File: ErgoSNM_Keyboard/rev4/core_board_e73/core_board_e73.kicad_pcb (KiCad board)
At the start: 2 copper layers, 68.5 x 53 mm, 60 parts, among them J1 USB_C_Receptacle_USB2.0, J2 Conn_02x10_Odd_Even, J3 Conn_02x10_Odd_Even, J4 PJ-393_TRRS_8P, J5 PJ-393_TRRS_8P, J6 Conn_Batt, J7 Debug, J8 Conn_02x05_Odd_Even, J9 Conn_02x05_Odd_Even, SW1 SW_SPDT, SW2 SW_SPDT, U1 E73-2G4M08S1C, U2 USBLC6-2SC6, U3 BQ24075RGT, U4 TPS63900, Y1 32.768kHz

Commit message: feat: update the connectors of the main board and core board
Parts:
- removed LD1: BLUE, LED_SMD:LED_0603_1608Metric
- removed LD2: RED, LED_SMD:LED_0603_1608Metric
- moved R11 24.9 mm to (133.5, 94.6), turned to 180 degrees
- moved R6 21.5 mm to (133.5, 95.8), turned to 180 degrees
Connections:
- J2 pad 18: unconnected-(J2-Pin_18-Pad18) -> CHG_LED
- J2 pad 2: unconnected-(J2-Pin_2-Pad2) -> STATUS_LED
- J2 pad 20: unconnected-(J2-Pin_20-Pad20) -> STATUS_LED
- J2 pad 4: unconnected-(J2-Pin_4-Pad4) -> CHG_LED
- R11 pad 1: VDDH -> CHG_LED
- R11 pad 2: Net-(LD2-A) -> Net-(U3-~{CHG})
- R6 pad 2: Net-(LD1-A) -> Net-(U1-P0.15)
- U1 pad 28: STATUS_LED -> Net-(U1-P0.15)
- U3 pad 9: Net-(LD2-K) -> Net-(U3-~{CHG})
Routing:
- net STATUS_LED: track 78.8 -> 16.6 mm, vias 2 -> 1
- net Net-(U3-~{CHG}): track 0.00 -> 27.4 mm, vias 0 -> 2
- net Net-(LD2-K): track 21.3 -> 0.00 mm, vias 2 -> 0
- net VDDH: track 25.8 -> 9.07 mm, vias 3 -> 2
- net Net-(U1-P0.15): track 0.00 -> 15.5 mm, vias 0 -> 2
- net CHG_LED: track 0.00 -> 15.3 mm, vias 0 -> 1
- net GND: track 42.0 -> 46.9 mm
- net Net-(LD2-A): track 1.40 -> 0.00 mm
- net Net-(LD1-A): track 1.36 -> 0.00 mm
- net COL_IO_5: track 20.0 -> 20.9 mm
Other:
- outline, holes or cut-outs redrawn

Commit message: feat: update E73 core board
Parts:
- removed H23, H5, H6, H7: MountingHole, ErgoSNM_Keyboard:mouse_bit
- removed H3, H4: MountingHole, MountingHole:MountingHole_2.7mm_M2.5_ISO7380
- removed J8, J9: Conn_02x05_Odd_Even, Connector_PinHeader_1.27mm:PinHeader_2x04_P1.27mm_Vertical
- removed the SB3 at (154.1, 92.6)
- removed the TP1 at (155.2, 117.8)
- added R14: 0R, Resistor_SMD:R_0603_1608Metric, F.Cu at (170.1, 103.3)
- added R15: 0R, Resistor_SMD:R_0603_1608Metric, F.Cu at (170.1, 101.8)
- added R18: 0R, Resistor_SMD:R_0603_1608Metric, F.Cu at (163.5, 119.1)
- added R8: 0R, Resistor_SMD:R_0603_1608Metric, F.Cu at (161.2, 104.1)
- added R9: 0R, Resistor_SMD:R_0603_1608Metric, F.Cu at (166.3, 108.2)
- added SB2: LiPo_CHG, Jumper:SolderJumper-2_P1.3mm_Open_TrianglePad1.0x1.5mm, B.Cu at (160.2, 102.6)
- J2, J3: footprint Connector_PinHeader_1.27mm:PinHeader_2x10_P1.27mm_Vertical_SMD -> Connector_PinHeader_1.27mm:PinHeader_2x10_P1.27mm_Vertical
- J7: footprint ErgoSNM_Keyboard:SWD 10pin -> Connector_PinHeader_1.27mm:PinHeader_2x05_P1.27mm_Vertical; moved to F.Cu
- R16: renamed from R12; value 1.2k 1% -> 15k 1%
- R19: renamed from R14; value 30k 1% -> 20k 1%
- SB3: renamed from SB2; value LiPo_CHG -> LiPo_BATT
- TP1: renamed from TP2; moved to F.Cu
- U1: footprint ErgoSNM_Keyboard:E73-2G4M08S1C-52840_PCBA -> ErgoSNM_Keyboard:E73-2G4M08S1C-52840_Hand
- moved R13 33.7 mm to (166.5, 101.1)
- moved C5 22.2 mm to (146.7, 123.7), turned to -90 degrees
- moved R19 22.0 mm to (159.4, 113.5)
- moved C11 21.8 mm to (163.5, 111.5)
- moved C12 21.8 mm to (163.5, 117.0)
- moved L1 21.8 mm to (167.1, 114.3)
- moved U4 21.8 mm to (163.5, 114.3)
- moved R17 21.8 mm to (159.4, 115.0)
- moved SB4 21.7 mm to (159.1, 114.2)
- moved R16 21.6 mm to (159.4, 116.5)
- moved C6 20.6 mm to (146.7, 121.6), turned to 90 degrees
- moved SB1 20.1 mm to (160.2, 105.4), turned to 180 degrees
- moved Y1 19.3 mm to (145.0, 122.7), turned to 90 degrees
- moved R10 18.8 mm to (146.2, 119.3), turned to -90 degrees
- moved R12 18.3 mm to (161.7, 106.4)
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- renumbered R8 to R10, R9 to R11, R10 to R12, R11 to R13, R13 to R17, R6 to R5, R5 to R6
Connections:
- net /CONN_D+ renamed /power/CONN_D+
- net /CONN_D- renamed /power/CONN_D-
- net /OUT_SEL renamed /power/OUT_SEL
- net /USB_SH renamed /power/USB_SH
- net /VBATT_SRC renamed /power/VBATT_SRC
- net /VIN_DCDC renamed /power/VIN_DCDC
- C12 pad 1: VDD -> /power/VOUT_DCDC
- C7 pad 1: VBUS -> Net-(SB2-A)
- U1 pad 10: COL_IO_2 -> COL_IO_0
- U1 pad 15: COL_IO_3 -> unconnected-(U1-P0.05-Pad15)
- U1 pad 17: COL_IO_4 -> unconnected-(U1-P1.09-Pad17)
- U1 pad 22: COL_IO_5 -> unconnected-(U1-P0.07-Pad22)
- U1 pad 30: HS_IO_4 -> HS_IO_1
- U1 pad 32: HS_IO_3 -> HS_IO_2
- U1 pad 34: HS_IO_2 -> HS_IO_3
- U1 pad 35: HS_IO_1 -> HS_IO_5
- U1 pad 36: HS_IO_5 -> HS_IO_4
- U1 pad 38: unconnected-(U1-P1.02-Pad38) -> COL_IO_3
- U1 pad 40: unconnected-(U1-P1.04-Pad40) -> COL_IO_4
- U1 pad 42: unconnected-(U1-P1.06-Pad42) -> COL_IO_5
- U1 pad 8: COL_IO_0 -> COL_IO_2
- U3 pad 13: VBUS -> Net-(SB2-A)
- U3 pad 15: GND -> Net-(U3-SYSOFF)
- U3 pad 4: GND -> Net-(U3-~{CE})
- U4 pad 6: VDD -> /power/VOUT_DCDC
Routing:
- net CHG_LED: track 15.3 -> 59.7 mm
- net ROW_IO_0: track 26.5 -> 58.8 mm
- net ROW_IO_1: track 25.6 -> 56.9 mm
- net ROW_IO_4: track 19.2 -> 50.0 mm
- net ROW_IO_5: track 17.8 -> 48.1 mm
- net ROW_IO_2: track 24.8 -> 55.0 mm
- net ROW_IO_3: track 23.9 -> 53.1 mm
- net RX: track 115.8 -> 86.7 mm, vias 4 -> 2
- net Net-(U3-~{CHG}): track 27.4 -> 1.62 mm, vias 2 -> 0
- net VDD: track 103.9 -> 129.5 mm, vias 3 -> 1
- net HS_IO_5: track 5.64 -> 30.1 mm
- net COL_IO_2: track 20.2 -> 43.1 mm
- net TX: track 117.6 -> 96.0 mm, vias 4 -> 2
- net RESET: track 57.0 -> 76.3 mm, vias 1 -> 4
- net COL_IO_1: track 20.8 -> 38.5 mm
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- added copper zone on F.Cu, net /power/VOUT_DCDC
- removed copper zone on F.Cu, net VDD
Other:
- board size 68.5 x 53 mm -> 48.3 x 49.5 mm
- board text added: "BAT"
- board text added: "ErgoSNM Rev4.0 Core Board (E73)"
- board text added: "USB"
- board text removed: "CHG"
- board text removed: "Core Board"
- board text removed: "ErgoSNM"
- board text removed: "L"
- board text removed: "OFF"
- board text removed: "ON"
- board text removed: "R"
- board text removed: "Rev${REVISION}"
- board text removed: "STA"
- board text removed: "Unit: mm"

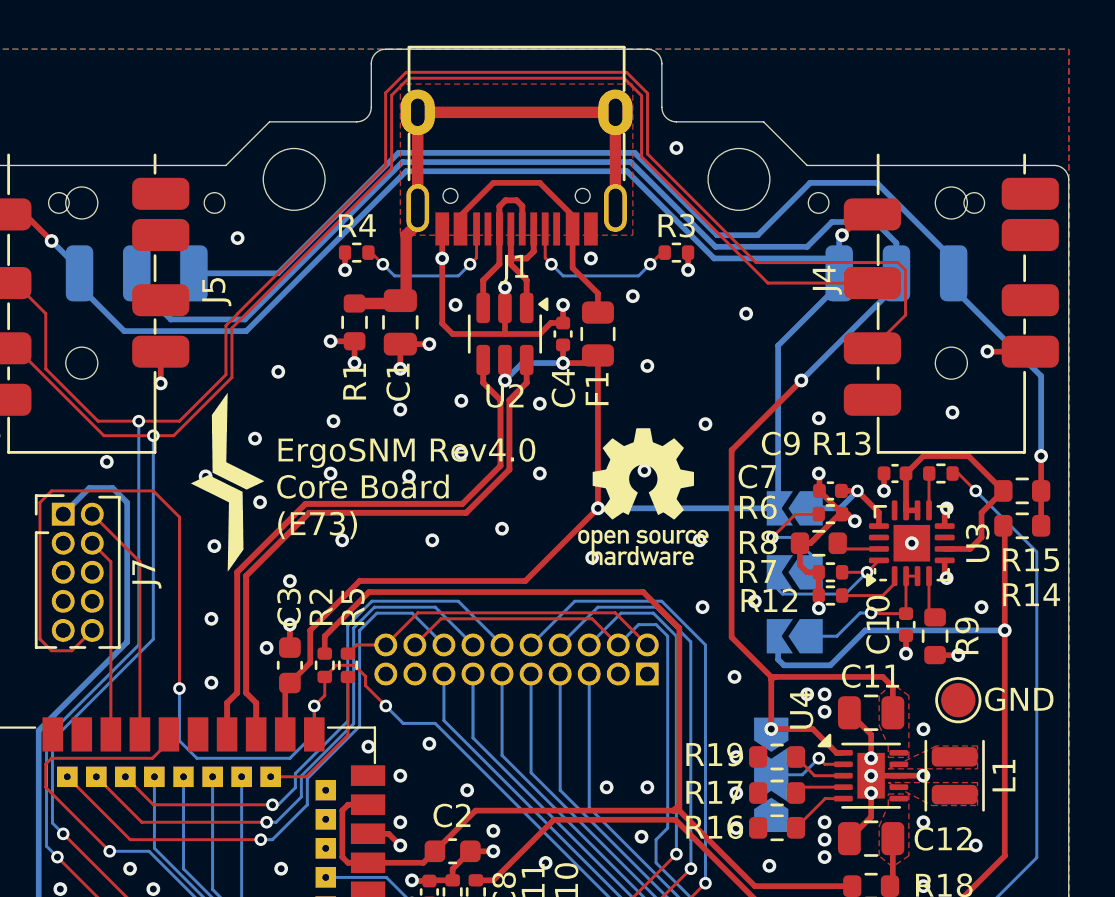
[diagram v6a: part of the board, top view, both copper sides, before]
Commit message: feat: add stats and change LED
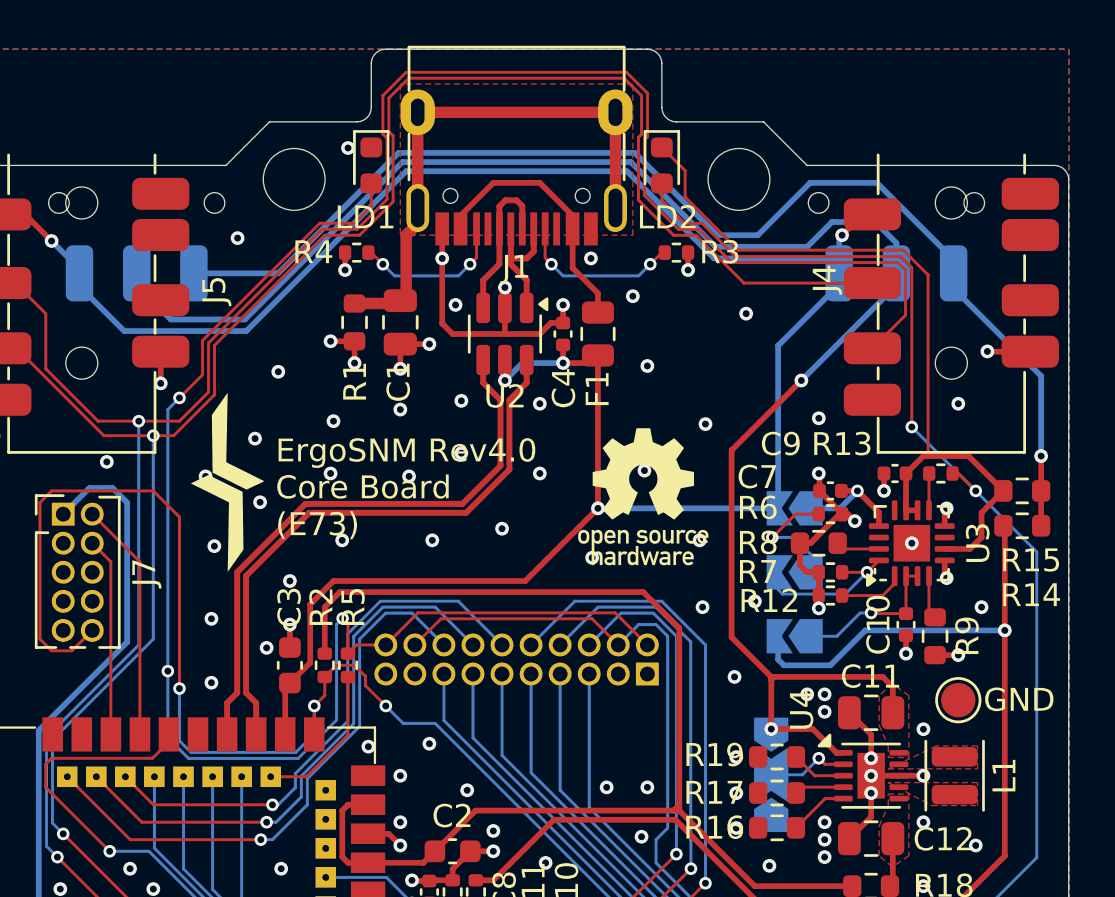
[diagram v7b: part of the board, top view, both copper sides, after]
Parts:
- added LD1: LED, LED_SMD:LED_0603_1608Metric, F.Cu at (141.7, 87.6)
- added LD2: LED, LED_SMD:LED_0603_1608Metric, F.Cu at (154.4, 87.6)
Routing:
- net STATUS_LED: track 14.4 -> 57.8 mm, vias 0 -> 3
- net CHG_LED: track 59.7 -> 83.5 mm, vias 1 -> 2
- net VDDH: track 11.6 -> 34.1 mm
- net RX: track 86.7 -> 89.0 mm
- net TX: track 96.0 -> 98.3 mm
- net VDD: track 129.5 -> 130.3 mm
- net VBUS: track 99.3 -> 100.0 mm
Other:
- board text added: "CHG"
- board text added: "STA"

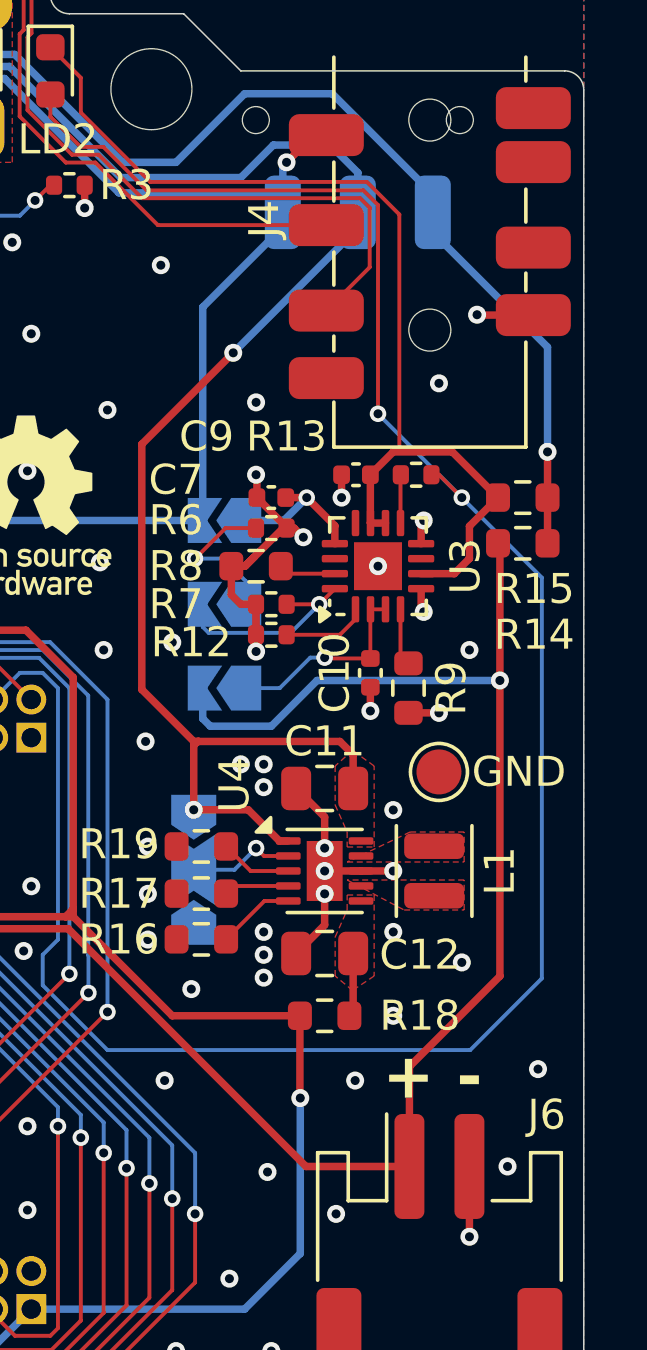
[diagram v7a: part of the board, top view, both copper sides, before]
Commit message: fix: add B5819 for battery reverse protection
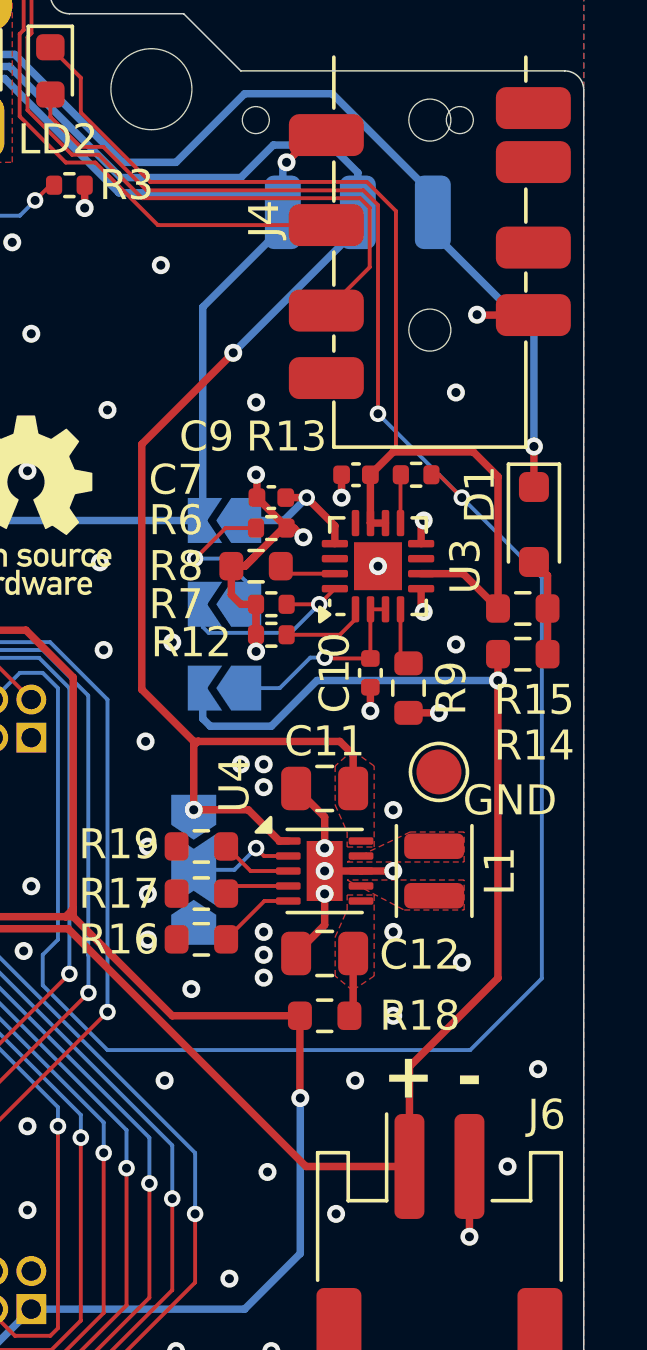
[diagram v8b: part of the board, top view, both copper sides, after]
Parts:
- added D1: B5819, Diode_SMD:D_SOD-323_HandSoldering, F.Cu at (170.5, 102.7)
- moved R14 3.70 mm to (170.1, 107.0)
- moved R15 3.70 mm to (170.1, 105.5)
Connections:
- R14 pad 2: /power/VBATT_SRC -> Net-(D1-A)
- R15 pad 2: /power/VBATT_SRC -> Net-(D1-A)
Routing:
- net +BATT: track 58.2 -> 54.4 mm
- net Net-(D1-A): track 0.00 -> 3.26 mm
- net VDDH: track 34.1 -> 37.1 mm
- net /power/VBATT_SRC: track 52.4 -> 50.4 mm
